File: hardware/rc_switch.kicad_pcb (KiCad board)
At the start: 2 copper layers, 35.6 x 22.9 mm, 9 parts, among them IC1 ATTINY85-P, P1 CONN_01X03, P2 CONN_01X04, P3 CONN_02X03, Q1 BUZ11, U1 ZTT8.00MT

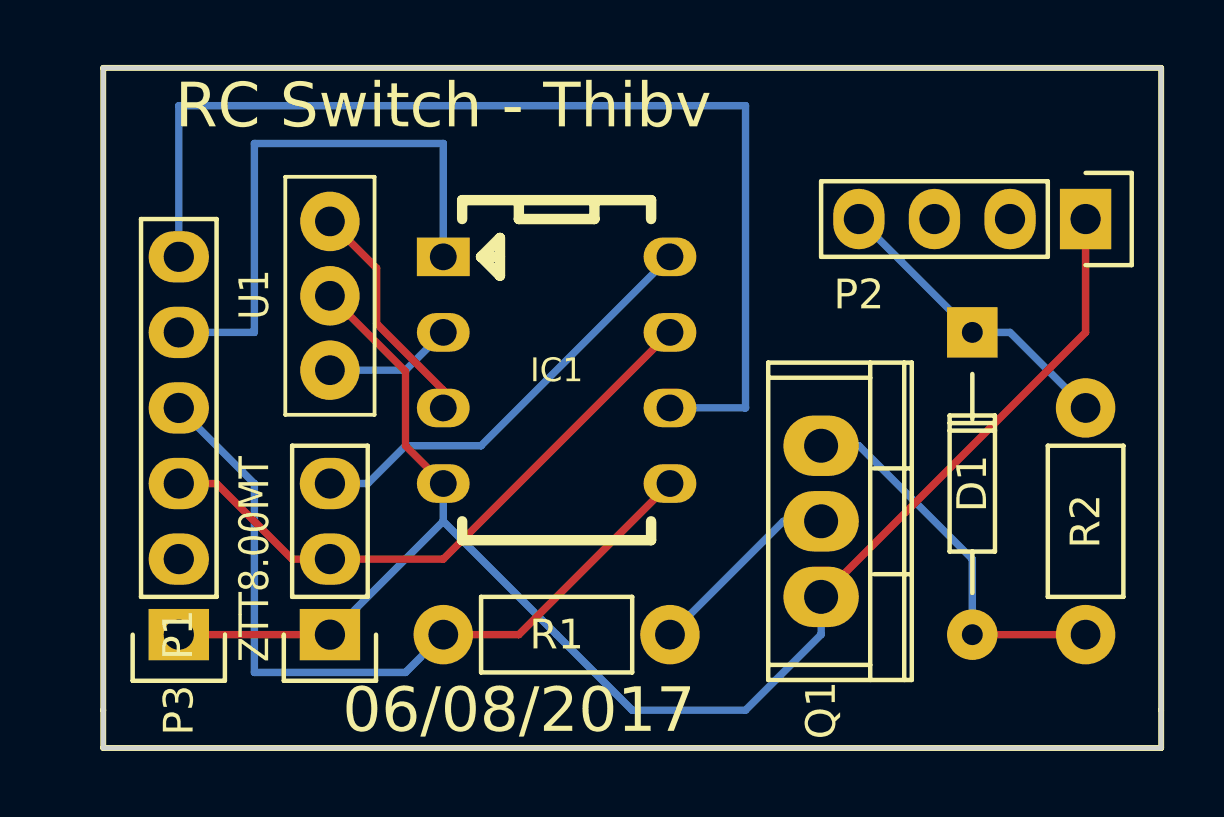
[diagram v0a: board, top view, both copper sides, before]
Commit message: Removing some components to keep only the strictly necessary parts. Adding mounting holes.
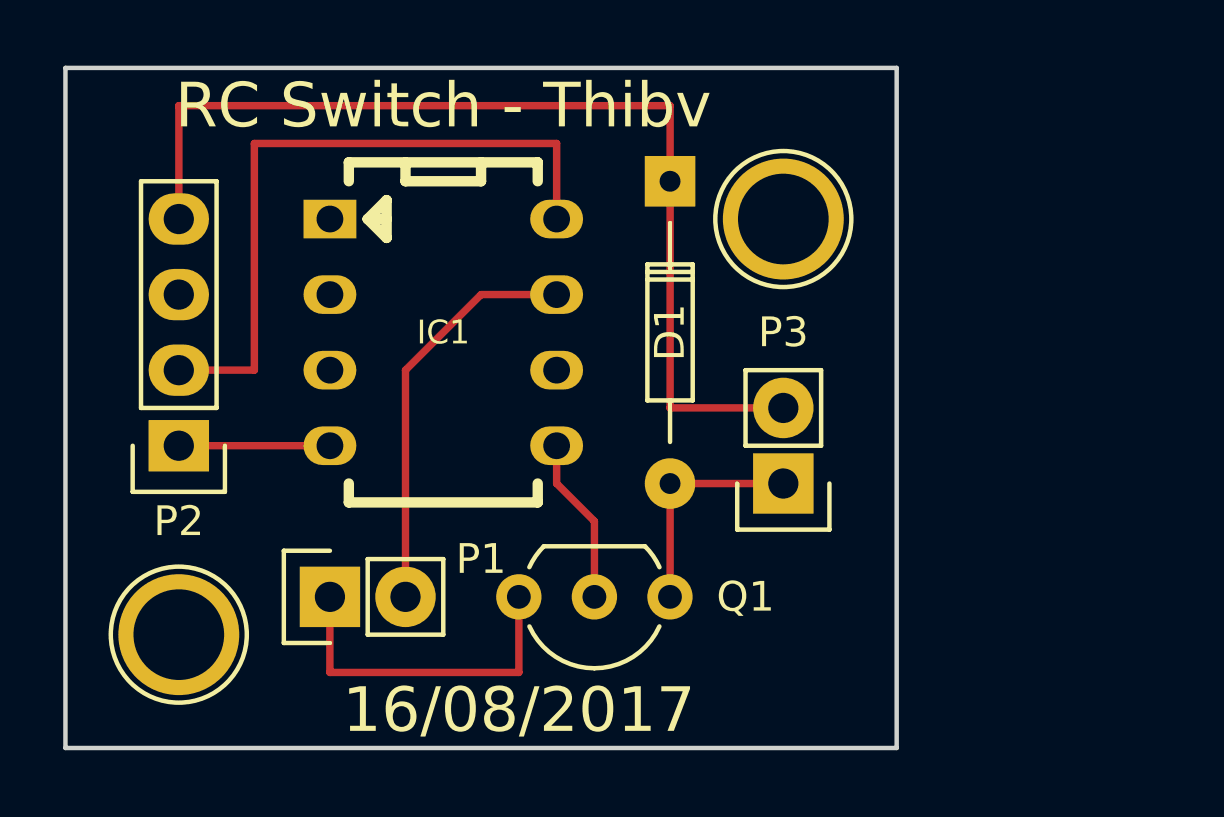
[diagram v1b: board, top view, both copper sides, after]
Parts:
- removed R1: 0, Resistors_ThroughHole:Resistor_Horizontal_RM7mm
- removed R2: LOAD, Resistors_ThroughHole:Resistor_Horizontal_RM7mm
- removed U1: ZTT8.00MT, ZTT8.00MT
- added REF**: 1pin, Connect:1pin, F.Cu at (134.6, 114.3)
- added REF**: 1pin, Connect:1pin, F.Cu at (154.9, 100.3)
- D1: value 1N4148 -> 1N4007
- P1: value CONN_01X03 -> CONN_01X02; footprint Socket_Strips:Socket_Strip_Straight_1x03 -> Socket_Strips:Socket_Strip_Straight_1x02
- P3: value CONN_02X03 -> CONN_01X02; footprint Socket_Strips:Socket_Strip_Straight_1x06 -> Socket_Strips:Socket_Strip_Straight_1x02
- Q1: value BUZ11 -> BS170; footprint TO-220 -> TO_SOT_Packages_THT:TO-92_Inline_Wide
- moved P2 31.4 mm to (134.6, 108.0), turned to 90 degrees
- moved P3 20.9 mm to (154.9, 109.2)
- moved D1 11.4 mm to (151.1, 99.1)
- moved Q1 5.68 mm to (151.1, 113.0), turned to 180 degrees
- moved IC1 4.02 mm to (143.5, 104.1)
- moved P1 1.27 mm to (139.7, 113.0), turned to 0 degrees
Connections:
- IC1 pad 1: /RST -> (no net)
- IC1 pad 2: Net-(IC1-Pad2) -> (no net)
- IC1 pad 3: Net-(IC1-Pad3) -> (no net)
- IC1 pad 6: /MISO -> (no net)
- IC1 pad 8: +5V -> /CELL1
- P2 pad 2: (no net) -> /CELL1
- P3 pad 1: GND -> Net-(D1-Pad2)
- P3 pad 2: (no net) -> /CELL3
- Q1 pad 2: Net-(Q1-Pad2) -> /CMD
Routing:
- net GND: track 53.7 -> 16.5 mm
- net /MISO: track 36.8 -> 0.00 mm
- net /CELL3: track 10.3 -> 34.3 mm
- net /CELL1: track 0.00 -> 22.9 mm
- net /CMD: track 26.5 -> 5.61 mm
- net /RST: track 19.0 -> 0.00 mm
- net +5V: track 14.6 -> 0.00 mm
- net Net-(IC1-Pad3): track 7.85 -> 0.00 mm
- net /RECEIVER: track 20.7 -> 13.8 mm
- net Net-(Q1-Pad2): track 6.66 -> 0.00 mm
- net Net-(D1-Pad2): track 13.0 -> 7.62 mm
- net Net-(IC1-Pad2): track 4.34 -> 0.00 mm
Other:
- board size 35.6 x 22.9 mm -> 27.9 x 22.9 mm
- board text added: "16/08/2017"
- board text removed: "06/08/2017"
